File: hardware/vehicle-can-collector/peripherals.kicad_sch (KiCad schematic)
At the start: 23 parts, among them J301 USB_B_Micro, J302 I2C_STANDARD, J303 Micro_SD_Card_Det, U301 FT2232HL, U302 93C56B, Y301 12MHz

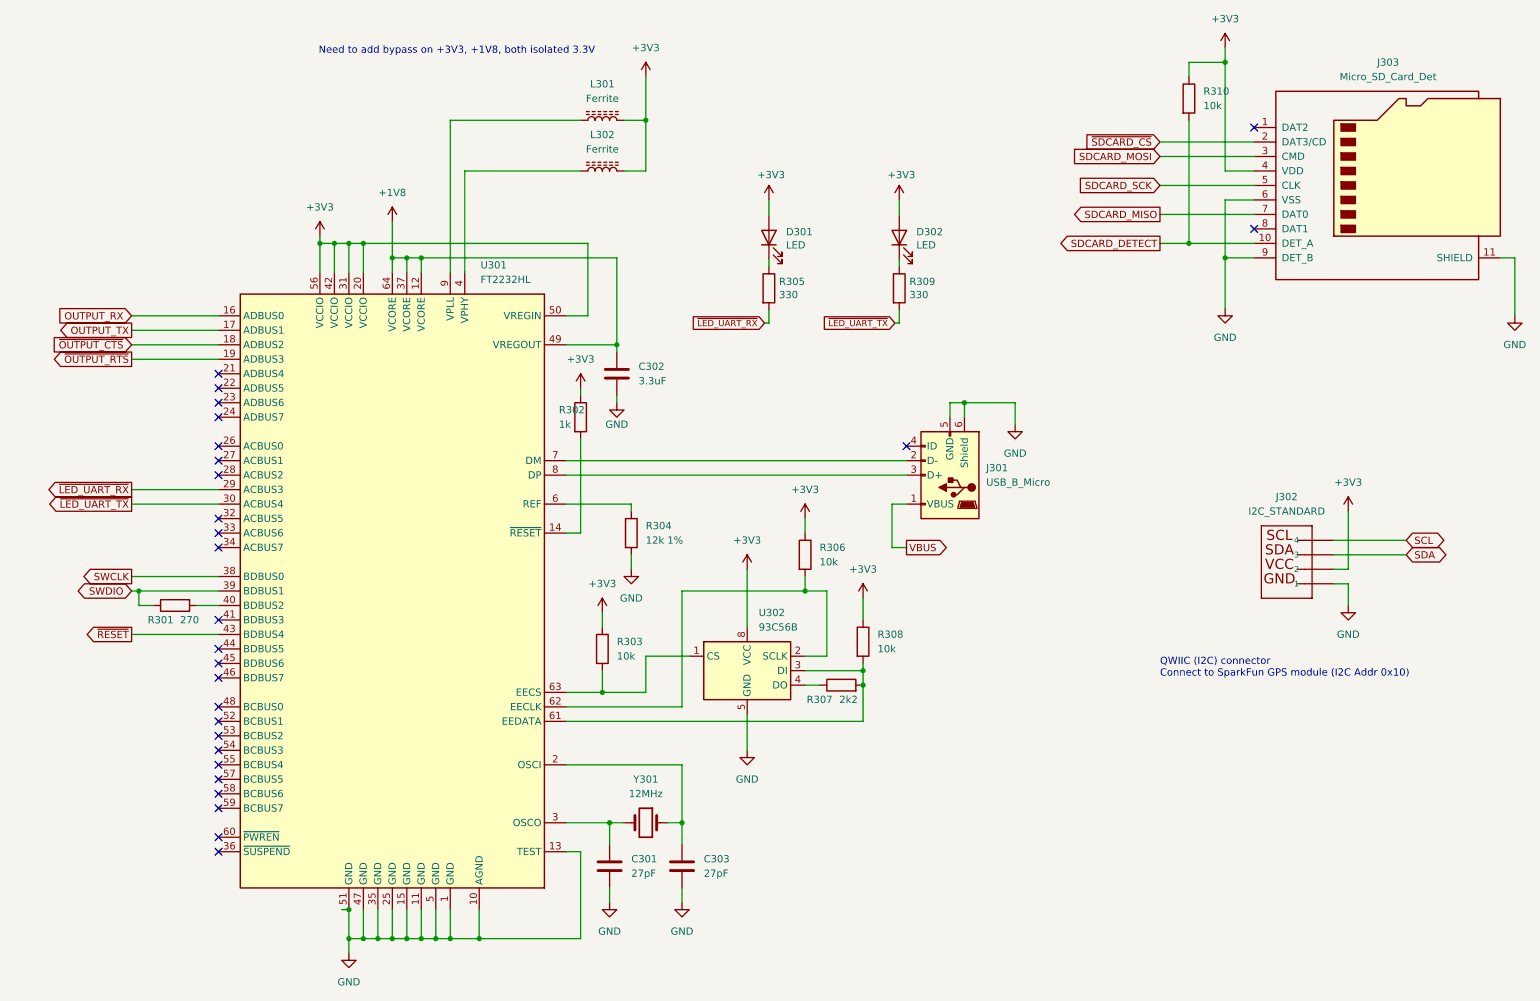
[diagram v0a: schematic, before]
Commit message: Added decoupling, more LEDs, update dts
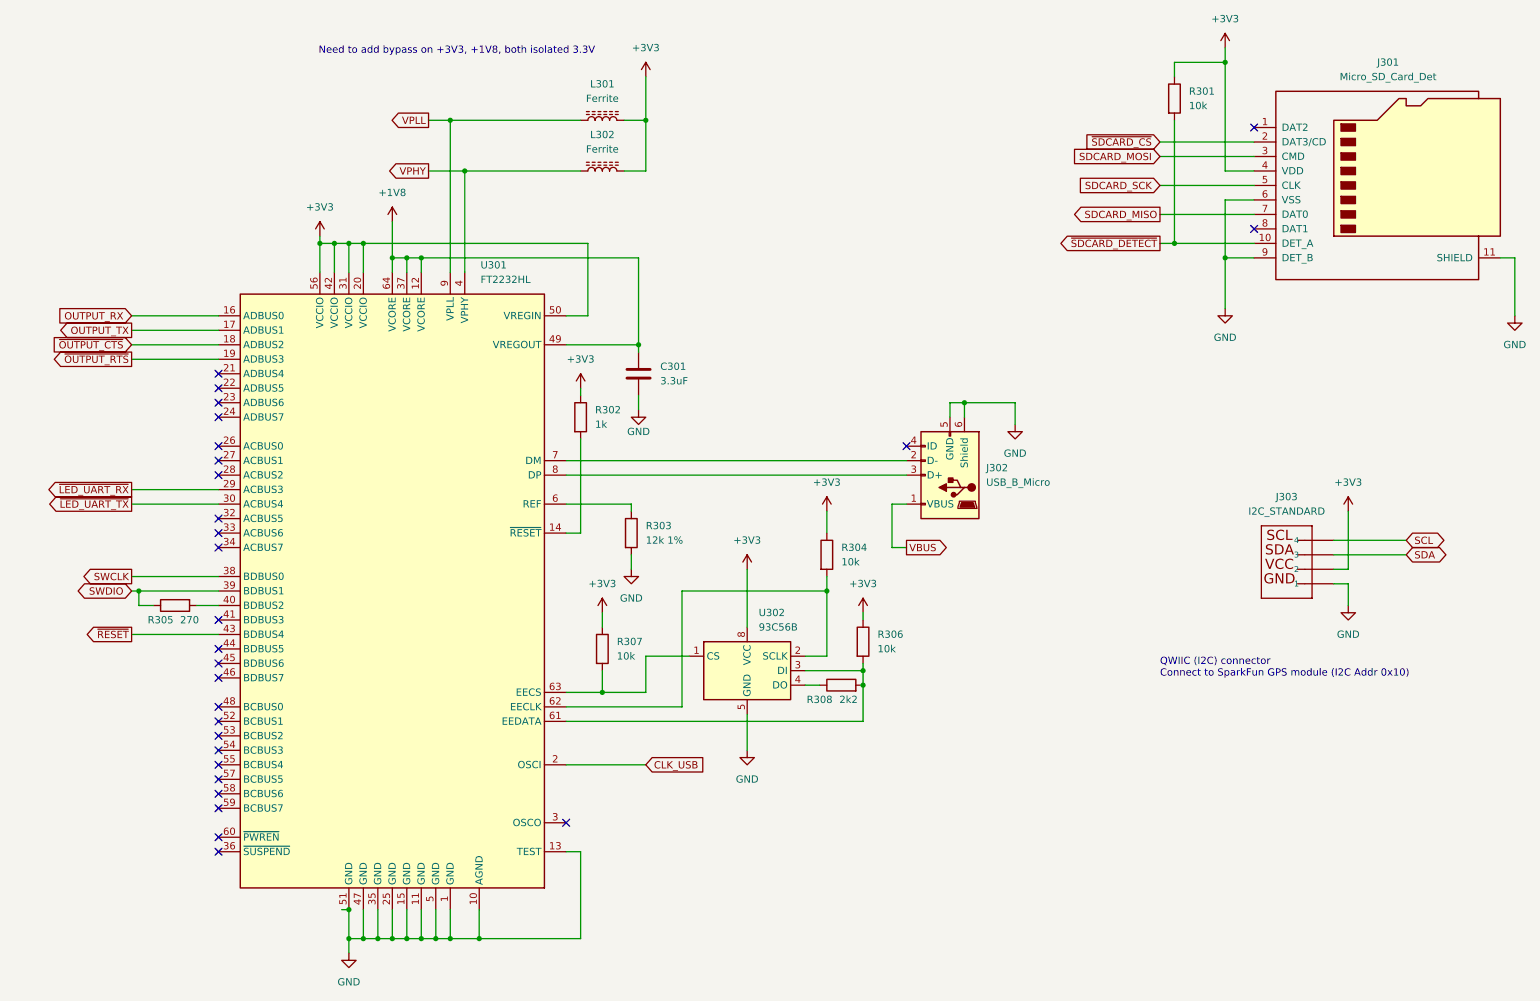
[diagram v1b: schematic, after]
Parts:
- removed C301, C303: 27pF, symbol Device:C
- removed D301, D302: LED, symbol Device:LED
- removed R305, R309: 330, symbol Device:R
- removed Y301: 12MHz, Crystal:Crystal_HC18-U_Horizontal, symbol Device:Crystal
- renumbered C302 to C301, J303 to J301, J301 to J302, J302 to J303, R310 to R301, R304 to R303, R306 to R304, R301 to R305, R308 to R306, R303 to R307, R307 to R308
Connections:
- net CLK_USB: now reaches U301.2 (OSCI)
- net VPHY: now reaches L302.1, U301.4 (VPHY)
- net VPLL: now reaches L301.1, U301.9 (VPLL)
- net SDCARD_DETECT renamed ~{SDCARD_DETECT}
- no-connect marks 27 -> 28
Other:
- company: (none) -> Gavin Hurlbut
- title: (none) -> Vehicle CAN Collector
- moved on the sheet: C301, R301, R304

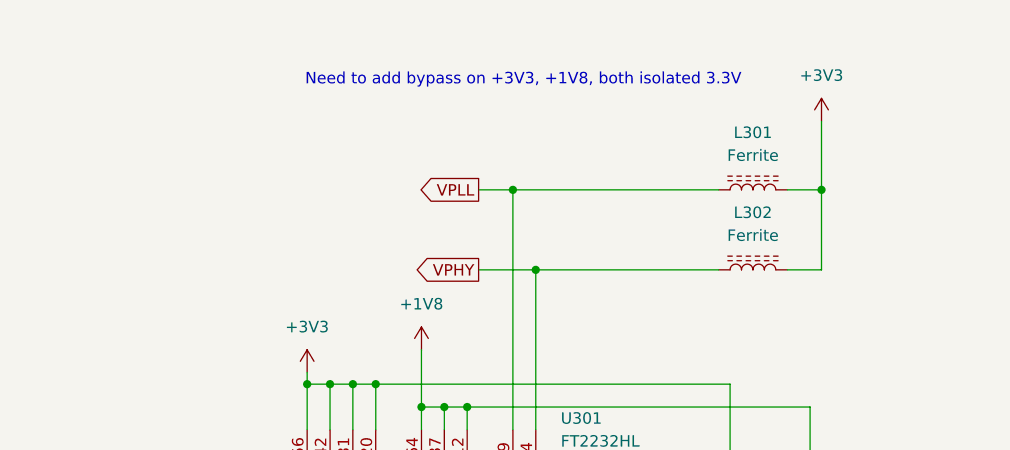
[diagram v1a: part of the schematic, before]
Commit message: Added footprints, tossed all footprints onto PCB
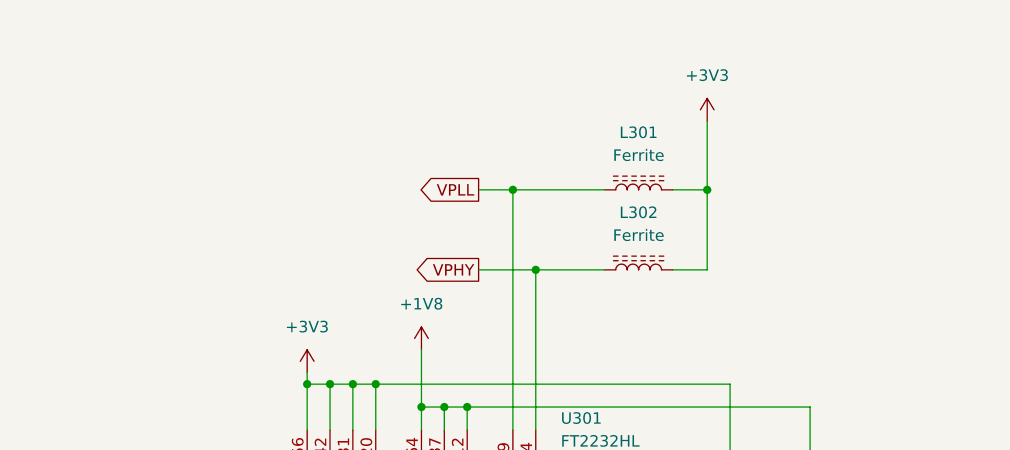
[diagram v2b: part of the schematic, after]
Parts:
- C301: footprint (none) -> Capacitor_SMD:C_0805_2012Metric_Pad1.18x1.45mm_HandSolder
- R301, R302, R303, R304, R305, R306, R307, R308: footprint (none) -> Resistor_SMD:R_0805_2012Metric_Pad1.20x1.40mm_HandSolder
- U302: footprint Package_SO:SOIC-8_3.9x4.9mm_P1.27mm -> Package_SO:TSSOP-8_4.4x3mm_P0.65mm
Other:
- note removed: "Need to add bypass on +3V3, +1V8, both isolated 3.3V"
- moved on the sheet: L301, L302
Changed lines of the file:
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@@
   (junction (at 72.39 64.77) (diameter 0) (color 0 0 0 0)
   )
+  (junction (at 109.22 43.18) (diameter 0) (color 0 0 0 0)
+  )
   (junction (at 214.63 64.77) (diameter 0) (color 0 0 0 0)
   )
@@
   )
   (junction (at 77.47 67.31) (diameter 0) (color 0 0 0 0)
-  )
-  (junction (at 121.92 43.18) (diameter 0) (color 0 0 0 0)
   )
   (junction (at 82.55 67.31) (diameter 0) (color 0 0 0 0)
@@
     (stroke (width 0) (type default) (color 0 0 0 0))
   )
-  (wire (pts (xy 121.92 52.07) (xy 118.11 52.07))
-    (stroke (width 0) (type default) (color 0 0 0 0))
-  )
   (wire (pts (xy 74.93 186.69) (xy 72.39 186.69))
     (stroke (width 0) (type default) (color 0 0 0 0))
@@
     (stroke (width 0) (type default) (color 0 0 0 0))
   )
+  (wire (pts (xy 109.22 43.18) (xy 109.22 52.07))
+    (stroke (width 0) (type default) (color 0 0 0 0))
+  )
   (wire (pts (xy 85.09 186.69) (xy 82.55 186.69))
     (stroke (width 0) (type default) (color 0 0 0 0))
@@
     (stroke (width 0) (type default) (color 0 0 0 0))
   )
-  (wire (pts (xy 121.92 43.18) (xy 118.11 43.18))
-    (stroke (width 0) (type default) (color 0 0 0 0))
-  )
   (wire (pts (xy 177.8 92.71) (xy 175.26 92.71))
     (stroke (width 0) (type default) (color 0 0 0 0))
   )
+  (wire (pts (xy 105.41 52.07) (xy 109.22 52.07))
+    (stroke (width 0) (type default) (color 0 0 0 0))
+  )
   (wire (pts (xy 77.47 67.31) (xy 77.47 69.85))
     (stroke (width 0) (type default) (color 0 0 0 0))
@@
     (stroke (width 0) (type default) (color 0 0 0 0))
   )
-  (wire (pts (xy 121.92 43.18) (xy 121.92 52.07))
+  (wire (pts (xy 109.22 35.56) (xy 109.22 43.18))
     (stroke (width 0) (type default) (color 0 0 0 0))
   )
@@
     (stroke (width 0) (type default) (color 0 0 0 0))
   )
-  (wire (pts (xy 121.92 35.56) (xy 121.92 43.18))
-    (stroke (width 0) (type default) (color 0 0 0 0))
-  )
   (wire (pts (xy 77.47 60.96) (xy 77.47 67.31))
     (stroke (width 0) (type default) (color 0 0 0 0))
@@
     (stroke (width 0) (type default) (color 0 0 0 0))
   )
-  (wire (pts (xy 87.63 43.18) (xy 110.49 43.18))
+  (wire (pts (xy 87.63 43.18) (xy 97.79 43.18))
     (stroke (width 0) (type default) (color 0 0 0 0))
   )
@@
     (stroke (width 0) (type default) (color 0 0 0 0))
   )
+  (wire (pts (xy 105.41 43.18) (xy 109.22 43.18))
+    (stroke (width 0) (type default) (color 0 0 0 0))
+  )
   (wire (pts (xy 160.02 142.24) (xy 160.02 148.59))
     (stroke (width 0) (type default) (color 0 0 0 0))
@@
     (stroke (width 0) (type default) (color 0 0 0 0))
   )
-  (wire (pts (xy 90.17 52.07) (xy 110.49 52.07))
+  (wire (pts (xy 90.17 52.07) (xy 97.79 52.07))
     (stroke (width 0) (type default) (color 0 0 0 0))
   )
@@
   (wire (pts (xy 223.52 57.15) (xy 223.52 67.31))
     (stroke (width 0) (type default) (color 0 0 0 0))
-  )
-  (text "Need to add bypass on +3V3, +1V8, both isolated 3.3V"
-    (at 113.03 31.75 0)
-    (effects (font (size 1.27 1.27)) (justify right bottom))
   )
   (text "QWIIC (I2C) connector\nConnect to SparkFun GPS module (I2C Addr 0x10)"
@@
       (effects (font (size 1.27 1.27)) (justify left))
     )
-    (property "Footprint" "Package_SO:SOIC-8_3.9x4.9mm_P1.27mm" (id 2) (at 139.7 139.7 0)
+    (property "Footprint" "Package_SO:TSSOP-8_4.4x3mm_P0.65mm" (id 2) (at 139.7 139.7 0)
       (effects (font (size 1.27 1.27)) hide)
     )
@@
       (effects (font (size 1.27 1.27)) (justify left))
     )
-    (property "Footprint" "" (id 2) (at 112.522 135.89 90)
+    (property "Footprint" "Resistor_SMD:R_0805_2012Metric_Pad1.20x1.40mm_HandSolder" (id 2) (at 112.522 135.89 90)
       (effects (font (size 1.27 1.27)) hide)
     )
@@
     (pin "1")
   )
-  (symbol (lib_id "Device:L_Ferrite") (at 114.3 52.07 90) (unit 1)
-    (in_bom yes) (on_board yes) (fields_autoplaced)
-    (property "Reference" "L302" (id 0) (at 114.3 45.72 90))
-    (property "Value" "Ferrite" (id 1) (at 114.3 48.26 90))
-    (property "Footprint" "Inductor_SMD:L_0805_2012Metric_Pad1.05x1.20mm_HandSolder" (id 2) (at 114.3 52.07 0)
-      (effects (font (size 1.27 1.27)) hide)
-    )
-    (property "Datasheet" "~" (id 3) (at 114.3 52.07 0)
+  (symbol (lib_id "Device:L_Ferrite") (at 101.6 52.07 90) (unit 1)
+    (in_bom yes) (on_board yes) (fields_autoplaced)
+    (property "Reference" "L302" (id 0) (at 101.6 45.72 90))
+    (property "Value" "Ferrite" (id 1) (at 101.6 48.26 90))
+    (property "Footprint" "Inductor_SMD:L_0805_2012Metric_Pad1.05x1.20mm_HandSolder" (id 2) (at 101.6 52.07 0)
+      (effects (font (size 1.27 1.27)) hide)
+    )
+    (property "Datasheet" "~" (id 3) (at 101.6 52.07 0)
       (effects (font (size 1.27 1.27)) hide)
     )
@@
     (pin "1")
   )
-  (symbol (lib_id "power:+3V3") (at 121.92 35.56 0) (unit 1)
-    (in_bom yes) (on_board yes) (fields_autoplaced)
-    (property "Reference" "#PWR0302" (id 0) (at 121.92 39.37 0)
-      (effects (font (size 1.27 1.27)) hide)
-    )
-    (property "Value" "+3V3" (id 1) (at 121.92 30.48 0))
-    (property "Footprint" "" (id 2) (at 121.92 35.56 0)
-      (effects (font (size 1.27 1.27)) hide)
-    )
-    (property "Datasheet" "" (id 3) (at 121.92 35.56 0)
+  (symbol (lib_id "power:+3V3") (at 109.22 35.56 0) (unit 1)
+    (in_bom yes) (on_board yes) (fields_autoplaced)
+    (property "Reference" "#PWR0302" (id 0) (at 109.22 39.37 0)
+      (effects (font (size 1.27 1.27)) hide)
+    )
+    (property "Value" "+3V3" (id 1) (at 109.22 30.48 0))
+    (property "Footprint" "" (id 2) (at 109.22 35.56 0)
+      (effects (font (size 1.27 1.27)) hide)
+    )
+    (property "Datasheet" "" (id 3) (at 109.22 35.56 0)
       (effects (font (size 1.27 1.27)) hide)
     )
@@
       (effects (font (size 1.27 1.27)) (justify left))
     )
-    (property "Footprint" "" (id 2) (at 212.852 39.37 90)
+    (property "Footprint" "Resistor_SMD:R_0805_2012Metric_Pad1.20x1.40mm_HandSolder" (id 2) (at 212.852 39.37 90)
       (effects (font (size 1.27 1.27)) hide)
     )
@@
       (effects (font (size 1.27 1.27)) (justify left))
     )
-    (property "Footprint" "" (id 2) (at 117.602 115.57 90)
+    (property "Footprint" "Resistor_SMD:R_0805_2012Metric_Pad1.20x1.40mm_HandSolder" (id 2) (at 117.602 115.57 90)
       (effects (font (size 1.27 1.27)) hide)
     )
@@
       (effects (font (size 1.27 1.27)) (justify left))
     )
-    (property "Footprint" "" (id 2) (at 108.712 95.25 90)
+    (property "Footprint" "Resistor_SMD:R_0805_2012Metric_Pad1.20x1.40mm_HandSolder" (id 2) (at 108.712 95.25 90)
       (effects (font (size 1.27 1.27)) hide)
     )
@@
     (pin "2")
   )
-  (symbol (lib_id "Device:L_Ferrite") (at 114.3 43.18 90) (unit 1)
-    (in_bom yes) (on_board yes) (fields_autoplaced)
-    (property "Reference" "L301" (id 0) (at 114.3 36.83 90))
-    (property "Value" "Ferrite" (id 1) (at 114.3 39.37 90))
-    (property "Footprint" "Inductor_SMD:L_0805_2012Metric_Pad1.05x1.20mm_HandSolder" (id 2) (at 114.3 43.18 0)
-      (effects (font (size 1.27 1.27)) hide)
-    )
-    (property "Datasheet" "~" (id 3) (at 114.3 43.18 0)
+  (symbol (lib_id "Device:L_Ferrite") (at 101.6 43.18 90) (unit 1)
+    (in_bom yes) (on_board yes) (fields_autoplaced)
+    (property "Reference" "L301" (id 0) (at 101.6 36.83 90))
+    (property "Value" "Ferrite" (id 1) (at 101.6 39.37 90))
+    (property "Footprint" "Inductor_SMD:L_0805_2012Metric_Pad1.05x1.20mm_HandSolder" (id 2) (at 101.6 43.18 0)
+      (effects (font (size 1.27 1.27)) hide)
+    )
+    (property "Datasheet" "~" (id 3) (at 101.6 43.18 0)
       (effects (font (size 1.27 1.27)) hide)
     )
@@
       (effects (font (size 1.27 1.27)) (justify left))
     )
-    (property "Footprint" "" (id 2) (at 121.6152 91.44 0)
+    (property "Footprint" "Capacitor_SMD:C_0805_2012Metric_Pad1.18x1.45mm_HandSolder" (id 2) (at 121.6152 91.44 0)
       (effects (font (size 1.27 1.27)) hide)
     )
@@
       (effects (font (size 1.27 1.27)) (justify left))
     )
-    (property "Footprint" "" (id 2) (at 151.892 119.38 90)
+    (property "Footprint" "Resistor_SMD:R_0805_2012Metric_Pad1.20x1.40mm_HandSolder" (id 2) (at 151.892 119.38 90)
       (effects (font (size 1.27 1.27)) hide)
     )
@@
     (property "Reference" "R305" (id 0) (at 36.83 130.81 90))
     (property "Value" "270" (id 1) (at 41.91 130.81 90))
-    (property "Footprint" "" (id 2) (at 39.37 126.492 90)
+    (property "Footprint" "Resistor_SMD:R_0805_2012Metric_Pad1.20x1.40mm_HandSolder" (id 2) (at 39.37 126.492 90)
       (effects (font (size 1.27 1.27)) hide)
     )
@@
     (property "Reference" "R308" (id 0) (at 152.4 144.78 90))
     (property "Value" "2k2" (id 1) (at 157.48 144.78 90))
-    (property "Footprint" "" (id 2) (at 156.21 144.018 90)
+    (property "Footprint" "Resistor_SMD:R_0805_2012Metric_Pad1.20x1.40mm_HandSolder" (id 2) (at 156.21 144.018 90)
       (effects (font (size 1.27 1.27)) hide)
     )
@@
       (effects (font (size 1.27 1.27)) (justify left))
     )
-    (property "Footprint" "" (id 2) (at 158.242 134.62 90)
-      (effects (font (size 1.27 1.27)) hide)
-    )
+    (property "Footprint" "Resistor_SMD:R_0805_2012Metric_Pad1.20x1.40mm_HandSolder" (id 2) (at 158.242 134.62 90)
+      (effects (font (size 1.27 1.27)) hide)
+    )

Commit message: Finished first round of layout.
- dang this has a lot of parts!
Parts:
- added J304: M04JST, SparkFun-Connectors:1X04-1.5MM_JST, symbol SparkFun-Connectors:M04JST
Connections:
- net +3V3: now also J304.2
- net GND: now also J304.1
- net OUTPUT_RX renamed ~{OUTPUT_RX}
- net OUTPUT_TX renamed ~{OUTPUT_TX}
- new net ~{LINBUS_RX}: J304.3
- new net ~{LINBUS_TX}: J304.4
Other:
- moved on the sheet: J303
